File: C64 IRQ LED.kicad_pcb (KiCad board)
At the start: 2 copper layers, 38.7 x 12.7 mm, 6 parts, among them J1 Signals, J2 ENABLE, U1 74LS04

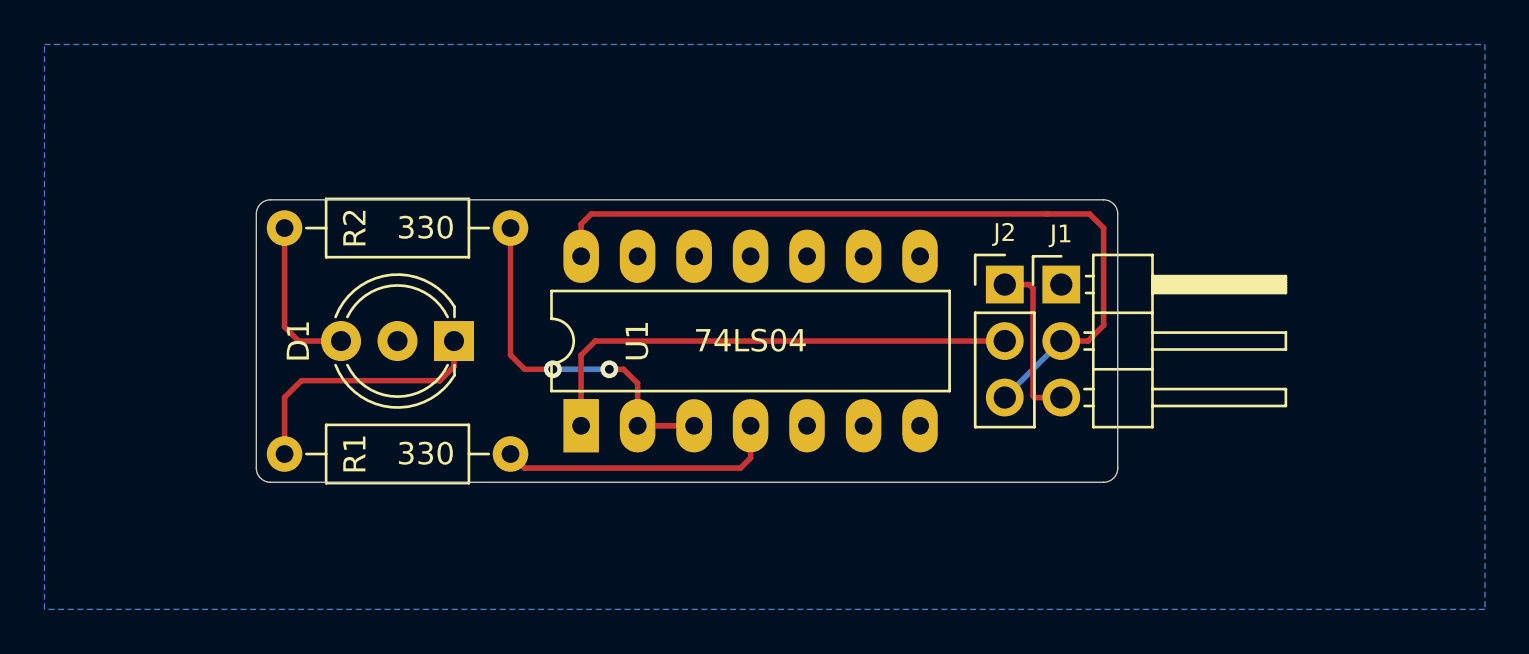
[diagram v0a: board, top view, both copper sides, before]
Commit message: Initial version of the Shift+IRQ LED MOD
adding Shift to the IRQ LED Mod
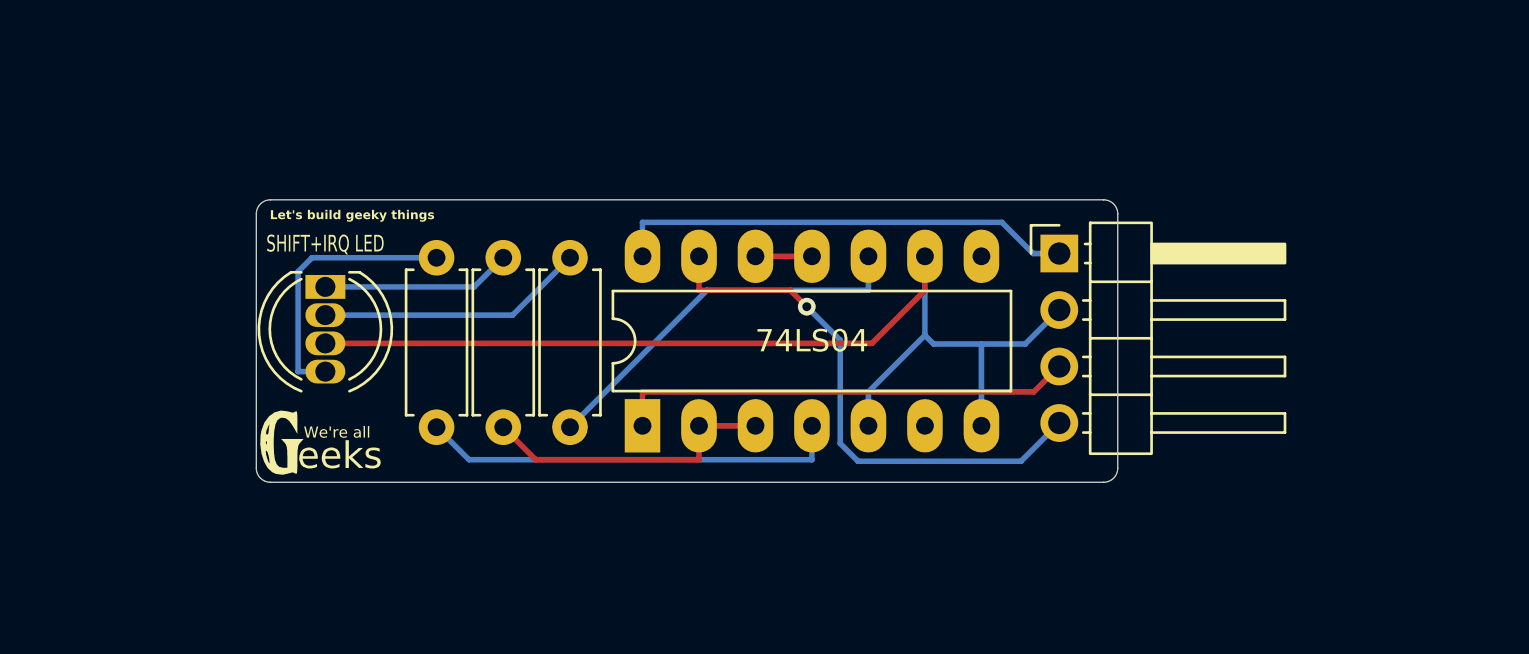
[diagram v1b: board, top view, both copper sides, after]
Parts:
- removed J2: ENABLE, Pin_Headers:Pin_Header_Straight_1x03_Pitch2.54mm
- added G***: LOGO, LOGO, F.Cu at (113.5, 119.5)
- added R3: 330, Resistor_THT:R_Axial_DIN0207_L6.3mm_D2.5mm_P7.62mm_Horizontal, F.Cu at (126.5, 118.8)
- D1: value Red/green LED -> RGB LED; footprint LEDs:LED_D5.0mm-3 -> LED_THT:LED_D5.0mm-4_RGB
- J1: footprint Pin_Headers:Pin_Header_Angled_1x03_Pitch2.54mm -> Connector_PinHeader_2.54mm:PinHeader_1x04_P2.54mm_Horizontal
- R1, R2: footprint Resistors_THT:R_Axial_DIN0207_L6.3mm_D2.5mm_P10.16mm_Horizontal -> Resistor_THT:R_Axial_DIN0207_L6.3mm_D2.5mm_P7.62mm_Horizontal
- moved R2 8.96 mm to (123.5, 118.8), turned to 90 degrees
- moved D1 6.28 mm to (115.5, 112.5), turned to -90 degrees
- moved R1 3.54 mm to (120.5, 118.8), turned to 90 degrees
- moved U1 2.76 mm to (129.8, 118.7)
- moved J1 1.40 mm to (148.5, 111.0)
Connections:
- D1 pad 1: Net-(D1-Pad1) -> Net-(D1-GA)
- D1 pad 2: GND -> Net-(D1-BA)
- D1 pad 3: Net-(D1-Pad3) -> GND
- J1 pad 1: GND -> VCC
- J1 pad 2: VCC -> GND
- J1 pad 3: Net-(J1-Pad3) -> Net-(J1-Pin_3)
- R1 pad 2: Net-(D1-Pad1) -> Net-(D1-RA)
- R2 pad 2: Net-(D1-Pad3) -> Net-(D1-GA)
- U1 pad 1: Net-(J2-Pad2) -> Net-(J1-Pin_3)
- U1 pad 10: (no net) -> Net-(R3-Pad1)
- U1 pad 11: GND -> Net-(U1-Pad11)
- U1 pad 12: (no net) -> Net-(U1-Pad11)
- U1 pad 13: GND -> Net-(J1-Pin_4)
- U1 pad 6: (no net) -> unconnected-(U1-Pad6)
- U1 pad 8: (no net) -> unconnected-(U1-Pad8)
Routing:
- net GND: track 0.00 -> 48.7 mm
- net Net-(J1-Pin_4): track 0.00 -> 24.3 mm, vias 0 -> 1
- net Net-(J2-Pad2): track 22.5 -> 0.00 mm
- net Net-(J1-Pin_3): track 0.00 -> 20.7 mm
- net Net-(R3-Pad1): track 0.00 -> 17.5 mm
- net VCC: track 35.6 -> 20.8 mm
- net Net-(D1-RA): track 0.00 -> 12.2 mm
- net Net-(D1-BA): track 0.00 -> 12.1 mm
- net Net-(D1-Pad1): track 11.9 -> 0.00 mm
- net Net-(D1-GA): track 0.00 -> 8.54 mm
- net Net-(J1-Pad3): track 7.48 -> 0.00 mm
- net Net-(D1-Pad3): track 7.25 -> 0.00 mm
- net Net-(R1-Pad1): track 12.7 -> 19.0 mm
- net Net-(R2-Pad1): track 16.4 -> 13.5 mm, vias 2 -> 0
- net Net-(U1-Pad11): track 0.00 -> 2.54 mm
- removed copper zone on B.Cu, net GND
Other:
- net class Default removed
- board text added: "G2-B3-GND-R1"
- board text added: "Let's build geeky things"
- board text added: "SHIFT+IRQ LED"
- board text added: "Shft-IRQ-GND-VCC"
- board text added: "We're all"
- board text added: "We're all geeks Shft+IRQ Derived from tebl/C64-IRQ-LED Licensed under CERN-OHL-S v2"
- board text added: "eeks"
- board text removed: "C64 IRQ LED github.com/tebl"
- board text removed: "EN"
- board text removed: "GND"
- board text removed: "GREEN"
- board text removed: "IRQ"
- board text removed: "RED"
- board text removed: "VCC"
